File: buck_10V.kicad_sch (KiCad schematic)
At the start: 41 parts, among them J301 Conn_02x02, Q301 MMBT5551, Q302 MMBT5551, Q303 LBSS84LT1G, U1301 LMR33630ADDA, U302 COS1333TR, U303 LMV321-TR

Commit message: Weeded out all ERC errors
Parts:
- added C1105, C1109: 10uF/50V, Capacitor_SMD:C_1206_3216Metric, symbol Device:C
- added U1102: H7533-H#, Package_TO_SOT_SMD:SOT-23, symbol Hatlabs:H7533-H#
- C1104: renamed from C1301; value 100nF 50V -> 100nF/50V; LCSC (none) -> C14663
- C1106: renamed from C1302; value 1uF 50V -> 1uF/50V; LCSC (none) -> C15849
- C1112: renamed from C1305; footprint PCM_Capacitor_SMD_AKL:C_0603_1608Metric -> Capacitor_SMD:C_0402_1005Metric; LCSC (none) -> C1525
- C1116: renamed from C1303; value 47uF 16V -> 47uF/16V
- C1117: renamed from C1304; value 47uF 16V -> 47uF/16V
- C301, C302: value 10uF 50V -> 10uF/50V
- C303: value 100nF 50V -> 100nF/50V; LCSC (none) -> C14663
- C309, C310: value 47uF 16V -> 47uF/16V
- C312: footprint PCM_Capacitor_SMD_AKL:C_0603_1608Metric -> Capacitor_SMD:C_0603_1608Metric; LCSC (none) -> C1671
- D305: LCSC C414017 -> C7420320
- R1106: renamed from R1301; LCSC (none) -> C25741
- R308: value 100R -> 120R; LCSC C25076 -> C25079
- R311: value 10k -> 15k; LCSC C25744 -> C25756
- R312: value 300k -> 680k; footprint PCM_Resistor_SMD_AKL:R_0603_1608Metric -> Resistor_SMD:R_0603_1608Metric; LCSC (none) -> C25822
- R313: value 39k -> 75k; footprint PCM_Resistor_SMD_AKL:R_0603_1608Metric -> Resistor_SMD:R_0603_1608Metric; LCSC (none) -> C23242
- U302: symbol SH-RPi:COS1333 -> Hatlabs:COS1333
- renumbered TP1301 to TP1102, U1301 to U1101
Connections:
- net B1_VIN: now also C1105.1, U1102.3 (IN)
- net GND: now also C1105.2, C1109.2, U1102.1 (GND)
- net CMx_3V3 renamed +3V3_LDO
- net +3V3_LDO: now also C1109.1, U1102.2 (OUT)
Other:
- note added: "FB voltage divider designed to have an 10.06V voltage at Vout"
- note added: "This LDO is required for circuits that need to be powered before the buck stages are online."
- note removed: "Buck filter design from RT6365 design tool"
- note removed: "FB voltage divider designed to have an 8.87V voltage at Vout"
- note removed: "FIXME: Check footprint"
- note removed: "FIXME: Check setpoint"
- company: Hat Labs Ltd -> Hat Labs Oy
- title: Sailor Hat for Raspberry Pi -> HALPI2
- moved on the sheet: C307, C311, D304, D305, R311, R314, U303

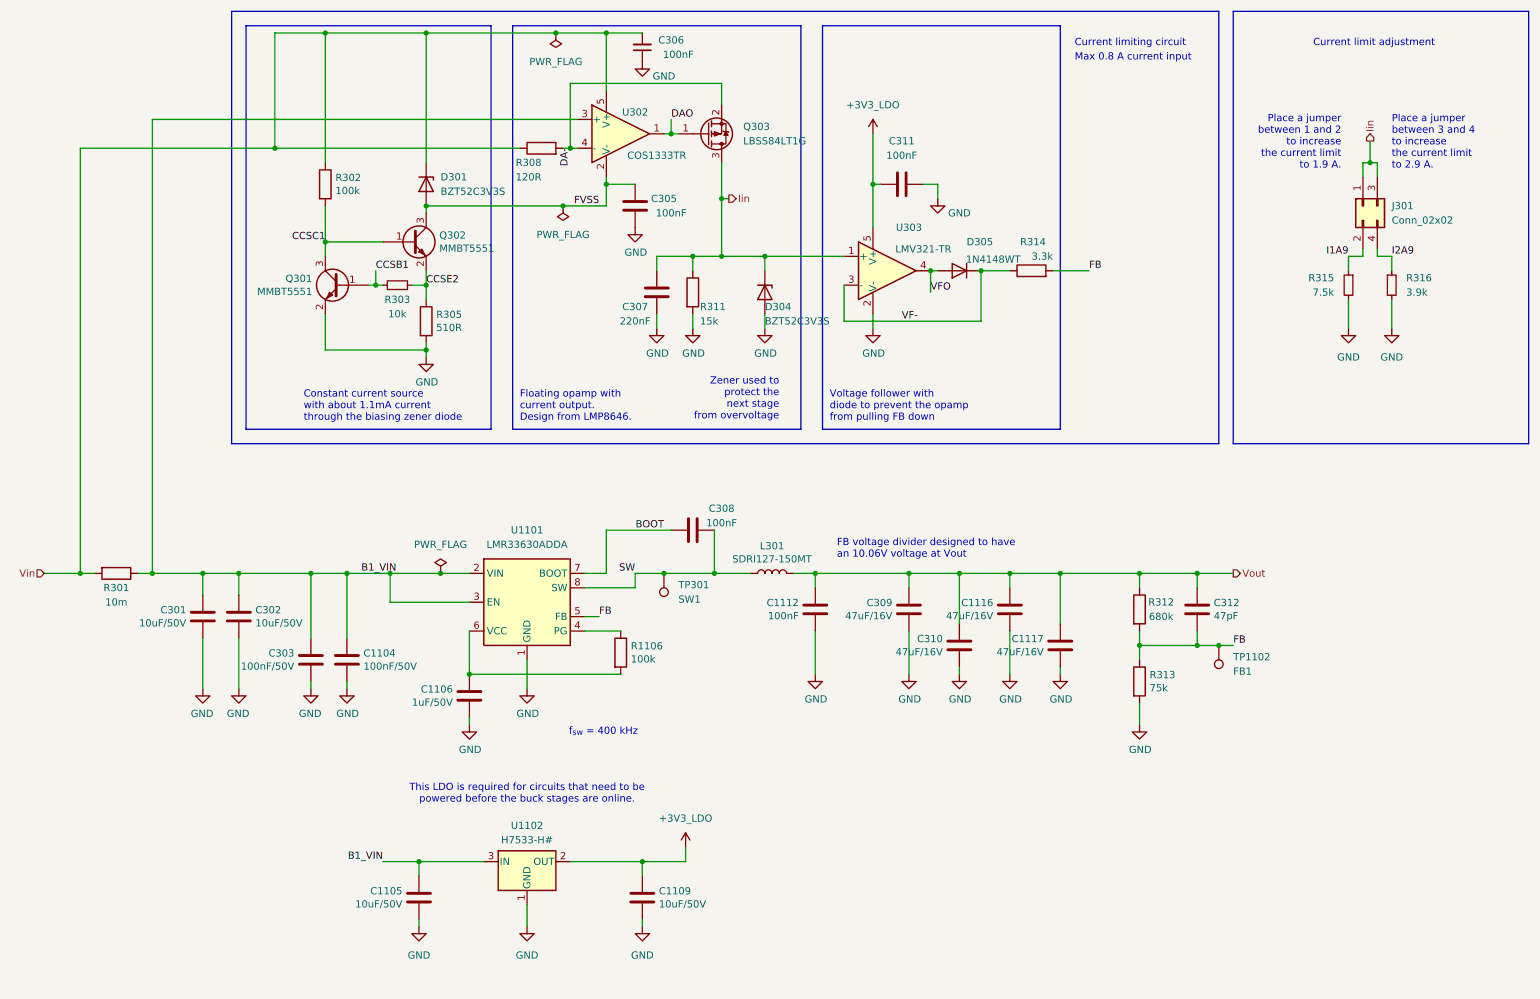
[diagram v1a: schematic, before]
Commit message: Implement ideal diodes for input and LDO power ORing
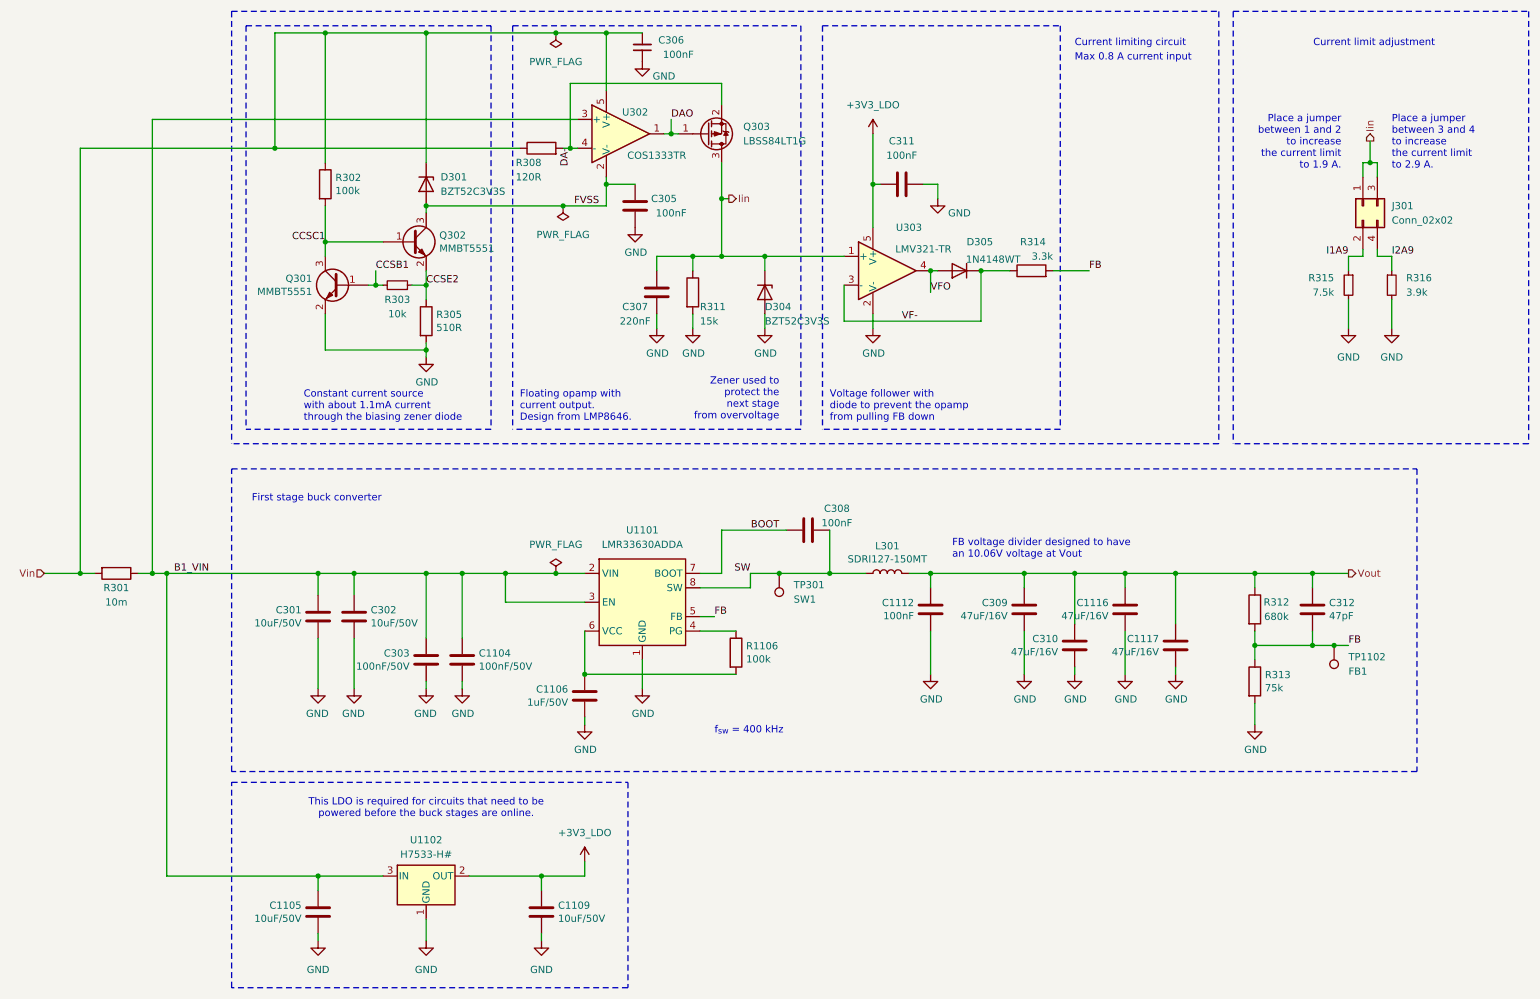
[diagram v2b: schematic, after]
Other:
- note added: "First stage buck converter"
- moved on the sheet: C1104, C1105, C1106, C1109, C1112, C1116, C1117, C301, C302, C303, C308, C309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

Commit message: Re-annotate schematics
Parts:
- renumbered C1105 to C1102, C1104 to C1105, C1109 to C1106, C1106 to C1107, C1112 to C1113, R1106 to R1107, U1102 to U1101, U1101 to U1103

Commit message: Sprinkle test points on the schematics
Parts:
- added TP1103, TP1104, TP1105, TP1106, TP1107: TestPoint, TestPoint:TestPoint_Pad_D1.0mm, symbol Connector:TestPoint
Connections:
- net +3V3_LDO: now also TP1105.1
- net B1_VIN: now also TP1104.1
- net FVSS: now also TP1106.1
- net Iin: now also TP1103.1
- net Vout: now also TP1107.1

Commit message: Partial trace layout, kick-ass custom rules
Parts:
- removed C1116, C1117, C310: 47uF/16V, Capacitor_SMD:C_1210_3225Metric, symbol Device:C
- C309: value 47uF/16V -> 220F/16V; footprint Capacitor_SMD:C_1210_3225Metric -> Capacitor_SMD:CP_Elec_6.3x7.7; symbol Device:C -> Device:C_Polarized; LCSC C77101 -> C5246526
- D301, D304: value BZT52C3V3S -> BZX584C3V3; footprint Diode_SMD:D_SOD-323 -> Diode_SMD:D_SOD-523; LCSC C173439 -> C19077462
- TP1306: renamed from TP1102; footprint TestPoint:TestPoint_Pad_D2.0mm -> TestPoint:TestPoint_Pad_D1.0mm
- TP301: footprint TestPoint:TestPoint_Pad_D2.0mm -> TestPoint:TestPoint_Pad_D1.0mm
- renumbered C1113 to C1306, C1105 to C1315, C1107 to C1316, C1102 to C1317, C1106 to C1318, R1107 to R1311, TP1106 to TP1301, TP1103 to TP1302, TP1104 to TP1303, TP1107 to TP1305, TP1105 to TP1307, U1103 to U1303, U1101 to U1304
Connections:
- net VCC: now reaches C1316.1, R1311.2, U1303.6 (VCC)
- net PG: now reaches R1311.1, U1303.4 (PG)
- net +3V3_LDO renamed +3.3VLDO

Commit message: A big part of layout and routing done
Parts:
- Q1302: renamed from Q302; Component Class (none) -> fine_pitch
- U1303: Component Class (none) -> fine_pitch
- renumbered C306 to C1301, C311 to C1302, C305 to C1303, C307 to C1304, C308 to C1305, C309 to C1307, C312 to C1309, C301 to C1310, C302 to C1311, C303 to C1314, D301 to D1301, D305 to D1302, D304 to D1303, J301 to J1301, L301 to L1301, Q303 to Q1301, Q301 to Q1303, R308 to R1301, R302 to R1302, R314 to R1303, R303 to R1304, R315 to R1305, R316 to R1306, R311 to R1307, R305 to R1308, R301 to R1309, R312 to R1310, R313 to R1312, TP301 to TP1304, U302 to U1301, U303 to U1302
